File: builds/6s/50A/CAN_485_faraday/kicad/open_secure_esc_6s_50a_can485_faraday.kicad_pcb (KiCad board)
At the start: 4 copper layers, 32 x 66.1 mm, 59 parts, among them J1 SolderPad_1x04_SMD_P1.27mm_Pr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, J2 SolderPad_1x02_SMD_P2.54mm, J3 SolderPad_1x02_SMD_P2.54mm, J4A SolderWirePad_1x01_SMD_5x10mm, J4B SolderWirePad_1x01_SMD_5x10mm, J4C SolderWirePad_1x01_SMD_5x10mm, J5A SolderWire-6sqmm_1x01_D3.5mm_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, J5B SolderWire-6sqmm_1x01_D3.5mm_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, Q1 Toshiba_2-5W1A_SOP-Advance-N_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, Q2 Toshiba_2-5W1A_SOP-Advance-N_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, Q3 Toshiba_2-5W1A_SOP-Advance-N_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, Q4 Toshiba_2-5W1A_SOP-Advance-N_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, Q5 Toshiba_2-5W1A_SOP-Advance-N_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, Q6 Toshiba_2-5W1A_SOP-Advance-N_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, U1 LQFP-64_10x10mm_P0.5mm, U2 Infineon_PG-USON-10-2-4_3x3mm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, U3 SOIC-20W_7.5x12.8mm_P1.27mm, U4 SOIC-20W_7.5x12.8mm_P1.27mm, U5 TI_RTA0040B_WQFN-40_6x6mm_P0.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, U6 SOIC-8_3.9x4.9mm_P1.27mm, U7 SOIC-8_3.9x4.9mm_P1.27mm, U8 SOIC-8_3.9x4.9mm_P1.27mm

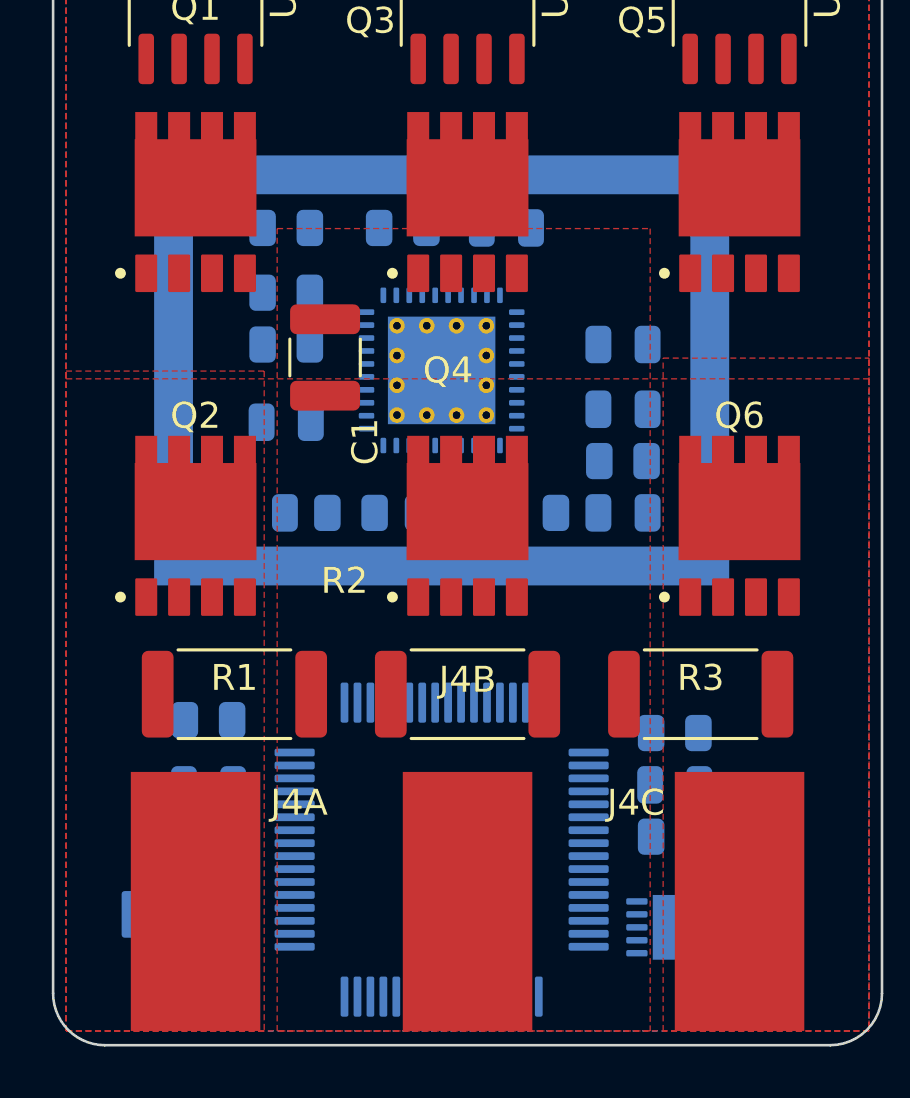
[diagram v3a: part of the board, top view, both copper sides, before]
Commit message: Verify the owner's U1/U5 centring; fix two defects it exposed
The repo owner moved U1 and U5 with their surrounding components +1.000 mm in
x, putting U1, U5 and SH1 exactly on the centreline. This is the move
symmetrize.py refused (DRC electrical 1 and 28) -- and the guard was right
about the tool's version, which moved the ICs ALONE. Moving each IC together
with its supporting parts is a different move, and it passes.

As saved the board showed 155 errors. All of them were stale zone fill; a
refill clears every one. Same lesson as the J5B move: a GUI part move leaves
the fill stale, so refill before judging the edit.

Board after refill: 17 violations, all warning severity, DRC electrical 0,
unconnected 157, creepage 7.83 mm, isolated lead 9.76 mm.

REAL COST, and the owner should have it explicitly: the worst gate loop grew
16.53 -> 17.36 mm, because centring the driver moves it away from phase A.
Per-phase driver-to-gate distance now Q1 12.17 / Q2 13.73 / Q3 6.85 /
Q4 5.89 / Q5 14.30 / Q6 14.86 mm. Centring did NOT balance A against C -- they
still differ by ~1.5 mm, because U5's gate pads are not symmetric on the
package. Symmetry was bought, phase balance was not.

TWO DEFECTS THE MOVE EXPOSED

remove_vm_island.py carried the island extent as a hardcoded rectangle,
measured once. When U5 moved, its via ring went with it and the rule area did
not, letting a 1.117 mm^2 sliver of VM plane escape through exactly the
millimetre no longer covered. The box is now derived from U5.41's actual via
positions on every run. A constant that describes another object's position
goes stale the moment that object moves -- this is the second such constant
found on this board.

tools/close_edge_orphans.py (new). The authored phase-terminal rule area
stopped at y 85.20 while the board outline runs to 86.05. Pour refilled that
0.85 mm gap and, cut off from above by the rule area itself, formed orphan
strips along the bottom edge on every layer -- including 8.747 mm^2 of GND on
In2.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
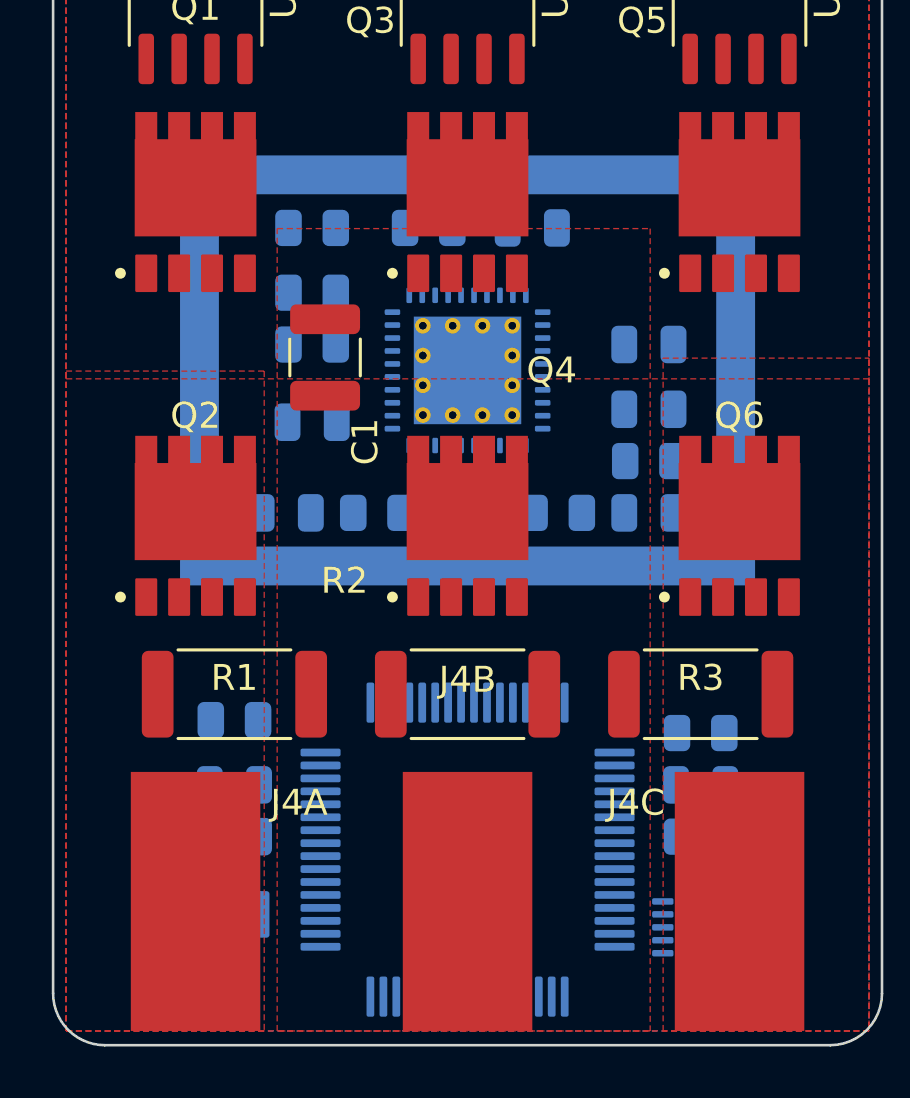
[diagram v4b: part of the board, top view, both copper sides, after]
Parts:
- moved R13 1.00 mm to (32.5, 65.5)
- moved C10 1.00 mm to (45.0, 76.0)
- moved C2 1.00 mm to (38.5, 54.5)
- moved C3 1.00 mm to (26.9, 78.0)
- moved C4 1.00 mm to (26.9, 76.0)
- moved C5 1.00 mm to (43.0, 59.0)
- moved C6 1.00 mm to (43.0, 61.5)
- moved C7 1.00 mm to (43.0, 65.5)
- moved C8 1.00 mm to (29.9, 62.0)
- moved C9 1.00 mm to (28.9, 65.5)
- moved J1 1.00 mm to (25.9, 81.0)
- moved R10 1.00 mm to (39.5, 65.5)
- moved R11 1.00 mm to (29.9, 57.0)
- moved R12 1.00 mm to (45.0, 74.0)
- moved R14 1.00 mm to (29.9, 59.0)
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
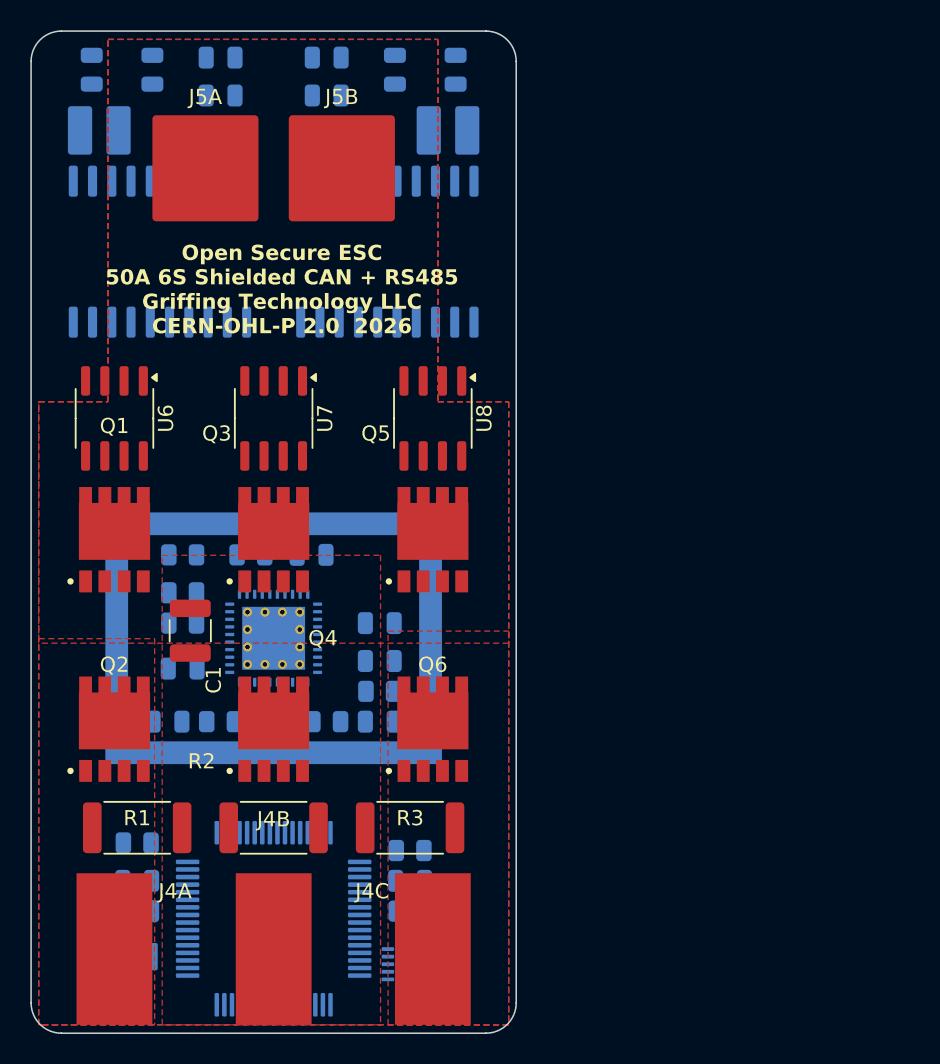
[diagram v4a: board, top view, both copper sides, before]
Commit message: Assembly prep for professional reflow; correct the routing state
The repo owner specified professional reflow assembly at JLCPCB or an
equivalent house. That decides one open question and exposes several more.

DECIDED: the five 0805 GND pads (C7 C9 C10 R5 R10) KEEP their solid zone
connections, and fix_starved_thermals.py --skip-passives is not to be used on
this build. A controlled reflow profile handles a solid 0805 GND bond; the
thermal relief was only ever worth it to protect hand-soldering and rework.
No change was needed -- the board was already in that state -- and TODO 12.5.ao
now says so, so nobody reverts it later.

CORRECTED, and it is the important one: THE BOARD IS NOT ROUTED. TODO 12.5.w
claimed "352 segments, 48 vias, 57 open". Measured, the board carries 0 track
segments, 2 vias and 157 unconnected items. Traced through history: 15eeaa4
("Route the signal nets") genuinely had 352 segments and 49 vias, and the very
next commit 8f4791a ("Repair the front/back re-placement") dropped it to 0 --
fix_after_replacement.py removed ALL routing, not only the stale segments its
message described. The board has been fully unrouted through every session
since, while the WBS kept describing the pre-repair state.

Nothing here can be fabricated or assembled until that is fixed. Creepage,
symmetry, thermals, fiducials and assembly attributes are all necessary and
none of them is sufficient.

tools/prep_for_assembly.py fixes three real assembly defects:

  * J1, J2 and J3 are bare wire/probe landing pads, like J4A/B/C and J5A/B,
    but unlike those were NOT excluded from the BOM and position files. They
    would have reached the assembler as parts to buy and place, for components
    that do not exist. Now flagged to match.
  * J5A/J5B carried no SMD/THT attribute -- convert_j5_to_smd.py changed the
    pads and not the attribute.
  * No fiducials existed on either side of a double-sided assembly (18
    footprints F.Cu, 41 B.Cu) carrying a 0.5 mm pitch WQFN-40 an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
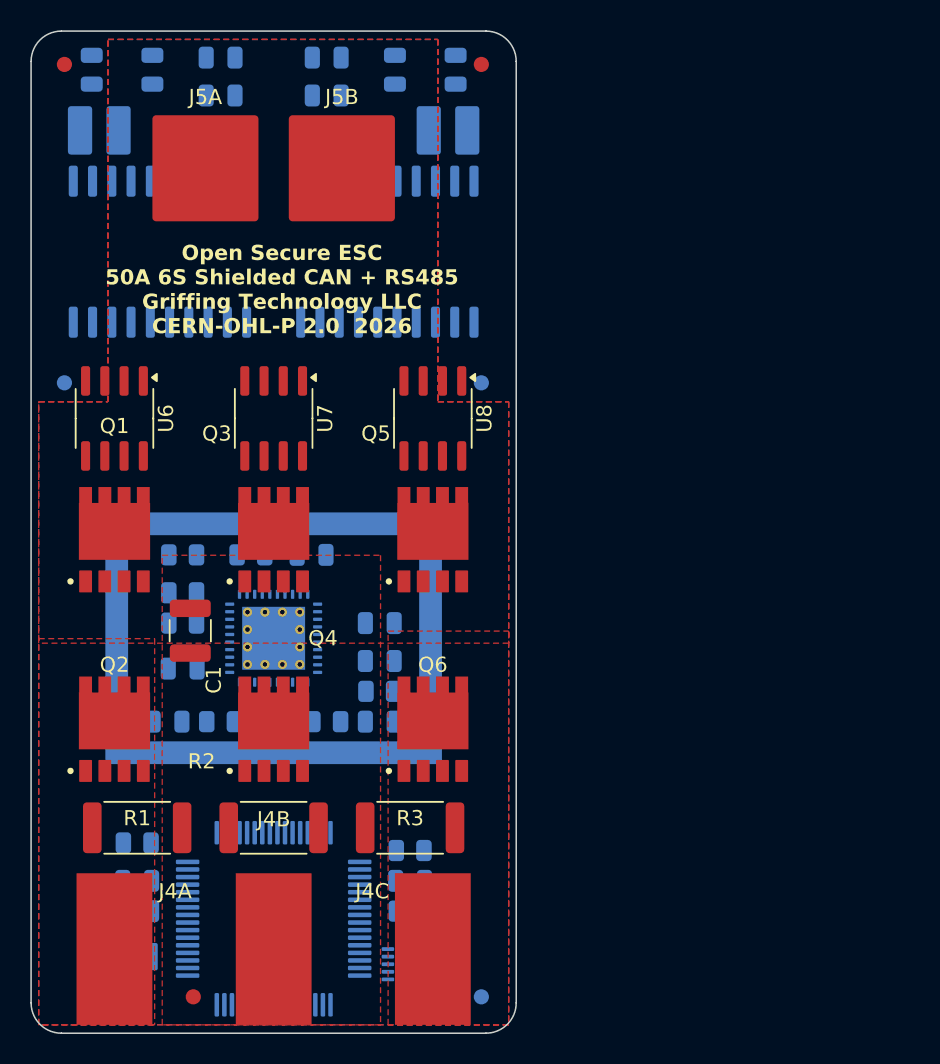
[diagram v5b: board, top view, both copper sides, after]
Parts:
- added FID1: Fiducial_1mm_Mask2mm, Fiducial_1mm_Mask2mm, F.Cu at (22.1, 22.1)
- added FID2: Fiducial_1mm_Mask2mm, Fiducial_1mm_Mask2mm, F.Cu at (49.6, 22.1)
- added FID3: Fiducial_1mm_Mask2mm, Fiducial_1mm_Mask2mm, F.Cu at (30.6, 83.7)
- added FID4: Fiducial_1mm_Mask2mm, Fiducial_1mm_Mask2mm, B.Cu at (22.1, 43.1)
- added FID5: Fiducial_1mm_Mask2mm, Fiducial_1mm_Mask2mm, B.Cu at (49.6, 43.1)
- added FID6: Fiducial_1mm_Mask2mm, Fiducial_1mm_Mask2mm, B.Cu at (49.6, 83.7)

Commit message: Routing pass: fix what the router was never told, and the pack return
The board was found fully unrouted (0 tracks, 0 vias, 157 ratsnest). Getting
it to route surfaced defects that were not routing defects, and every one of
them made the route look BETTER, so no completion metric could have caught
them.

Fixed in the KiCad->Specctra->FreeRouting handoff (tools/autoroute.py):
- net classes had vanished from the .kicad_pro, so VM, GND and all three motor
  phases would have routed at the 0.2 mm signal default. Now a hard stop.
- two class net names no longer existed (renamed by the ferrite respin) and
  silently matched nothing. Now a hard stop.
- KiCad exports every rule area as a TOTAL Specctra keepout, losing "tracks
  allowed". The isolation rule area therefore declared the band holding U1, U2
  and J1 unroutable on all four layers -- the MCU could not be connected, and
  it read as congestion. Pour-only keepouts are now stripped.
- KiCad exports In1.Cu/In2.Cu as (type signal). The first run cut 59 segments /
  196.7 mm of signal through the GND plane and 29 / 218.3 mm through the VM
  plane. Now marked (type power); verified 0 segments on both.
- autoroute.py cleared and SAVED the board before running the router, so a
  router hang left the real board wiped. It now writes the cleared board to
  scratch and only touches the project file once a result exists.

Board work:
- tools/fix_phase_pours.py: PH_A and PH_C stopped 3.04 mm short of their
  high-side FET source pads, splitting each half-bridge switch node in two.
  PH_B was correct, so the defect was not even symmetric.
- tools/stitch_planes.py: the board carried ZERO vias -- all four poured planes
  floating. In1.Cu (GND) and In2.Cu (VM) were poured, DRC-quiet, and tied to
  nothing.
- tools/split_top_pour.py: the 50 A pack return had no path to ground. J5B is
  F.Cu-only and F.Cu carries VM across the top, so its only route was a via --
  and a via there destroys the layer separation the isolation barrier is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
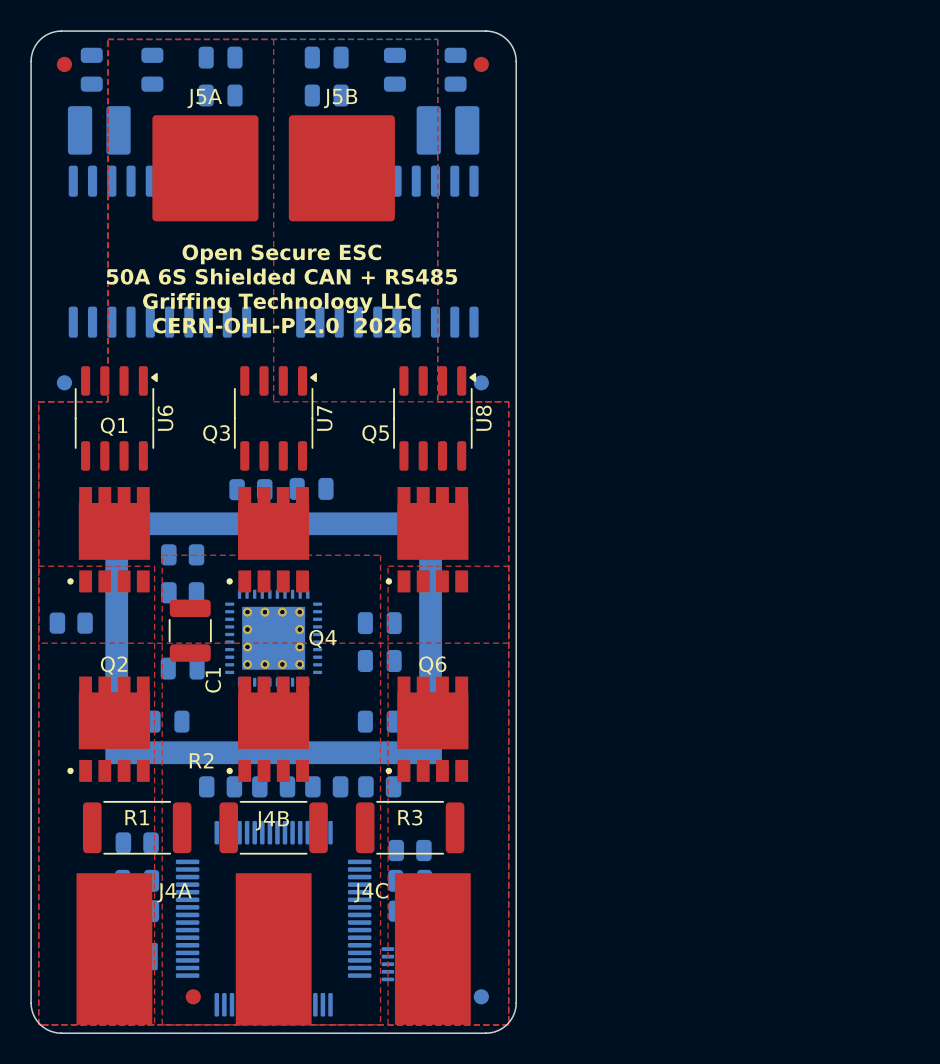
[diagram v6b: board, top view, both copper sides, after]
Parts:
- moved R14 7.35 mm to (22.6, 59.0)
- moved R4 6.30 mm to (43.0, 69.8)
- moved C2 4.35 mm to (38.5, 50.1)
- moved R10 4.30 mm to (39.5, 69.8)
- moved R13 4.30 mm to (32.5, 69.8)
- moved R5 4.30 mm to (36.0, 69.8)
- moved R6 4.30 mm to (34.5, 50.2)
